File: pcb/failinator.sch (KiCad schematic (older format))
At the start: 5 parts, among them P1 CONN_01X04, P4 CONN_01X06, U2 RASPIPLUSHEADER, U3 LDS-CD16RI, U4 LDS-CD16RI

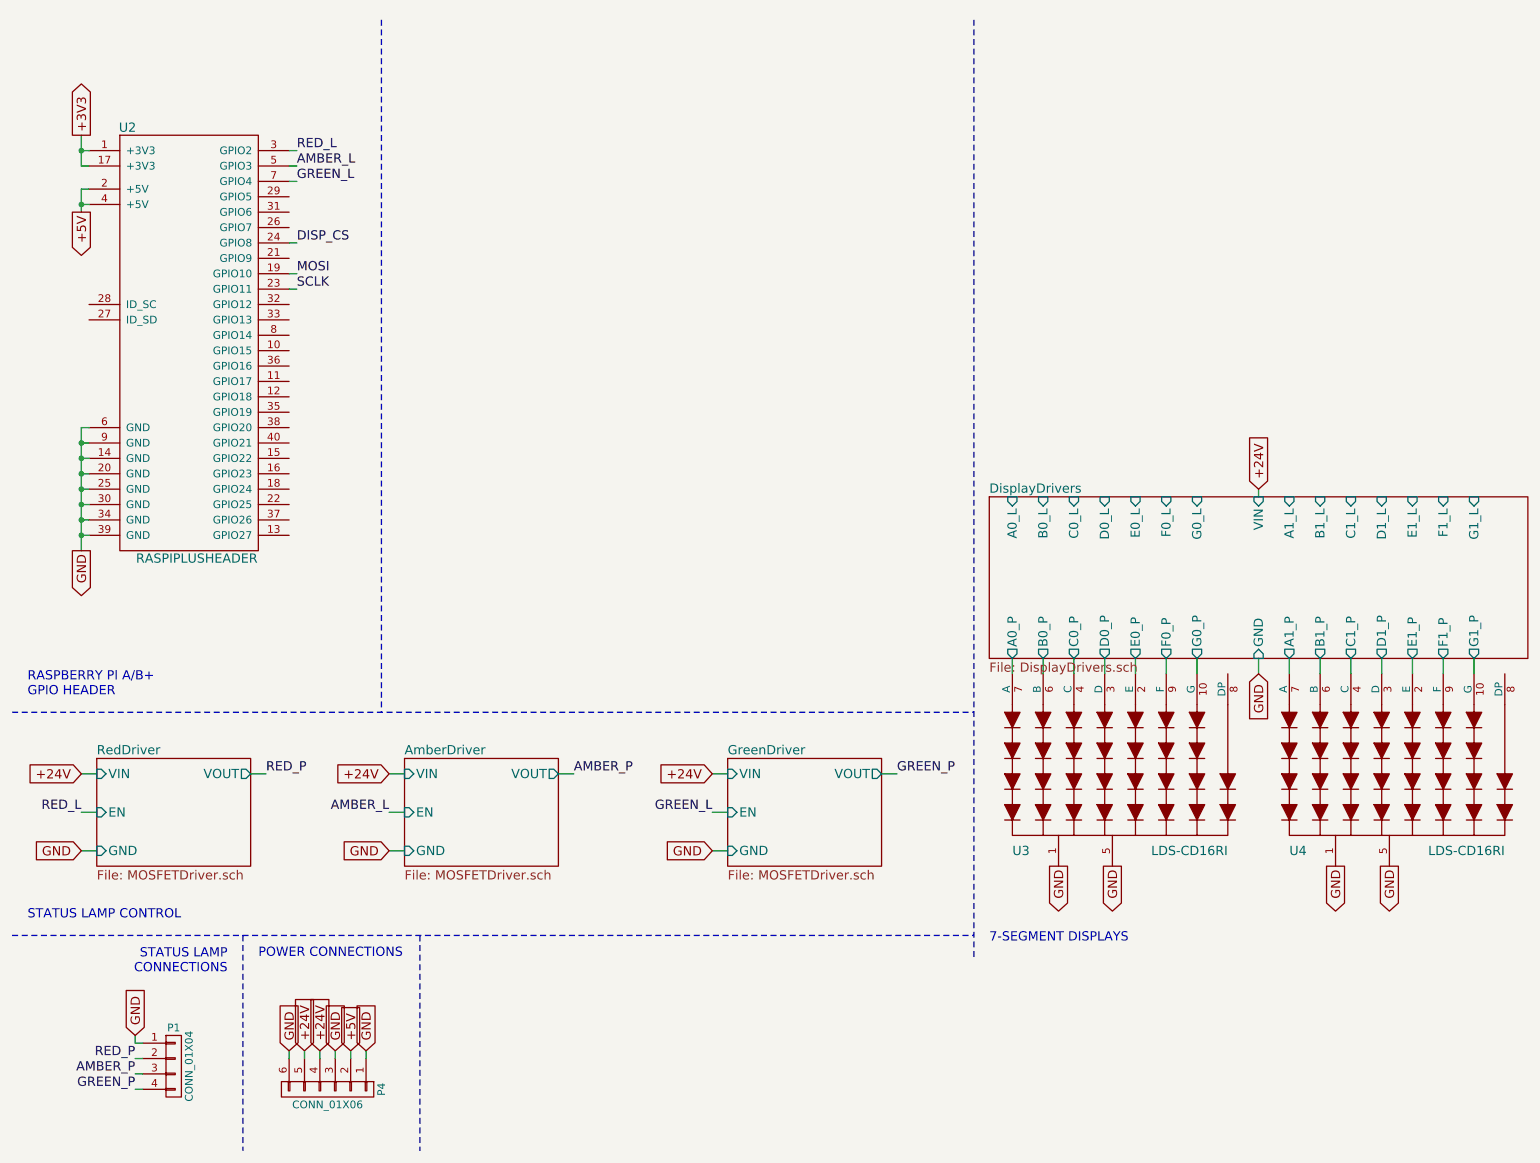
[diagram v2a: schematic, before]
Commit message: Shift registers for the 7-seg displays
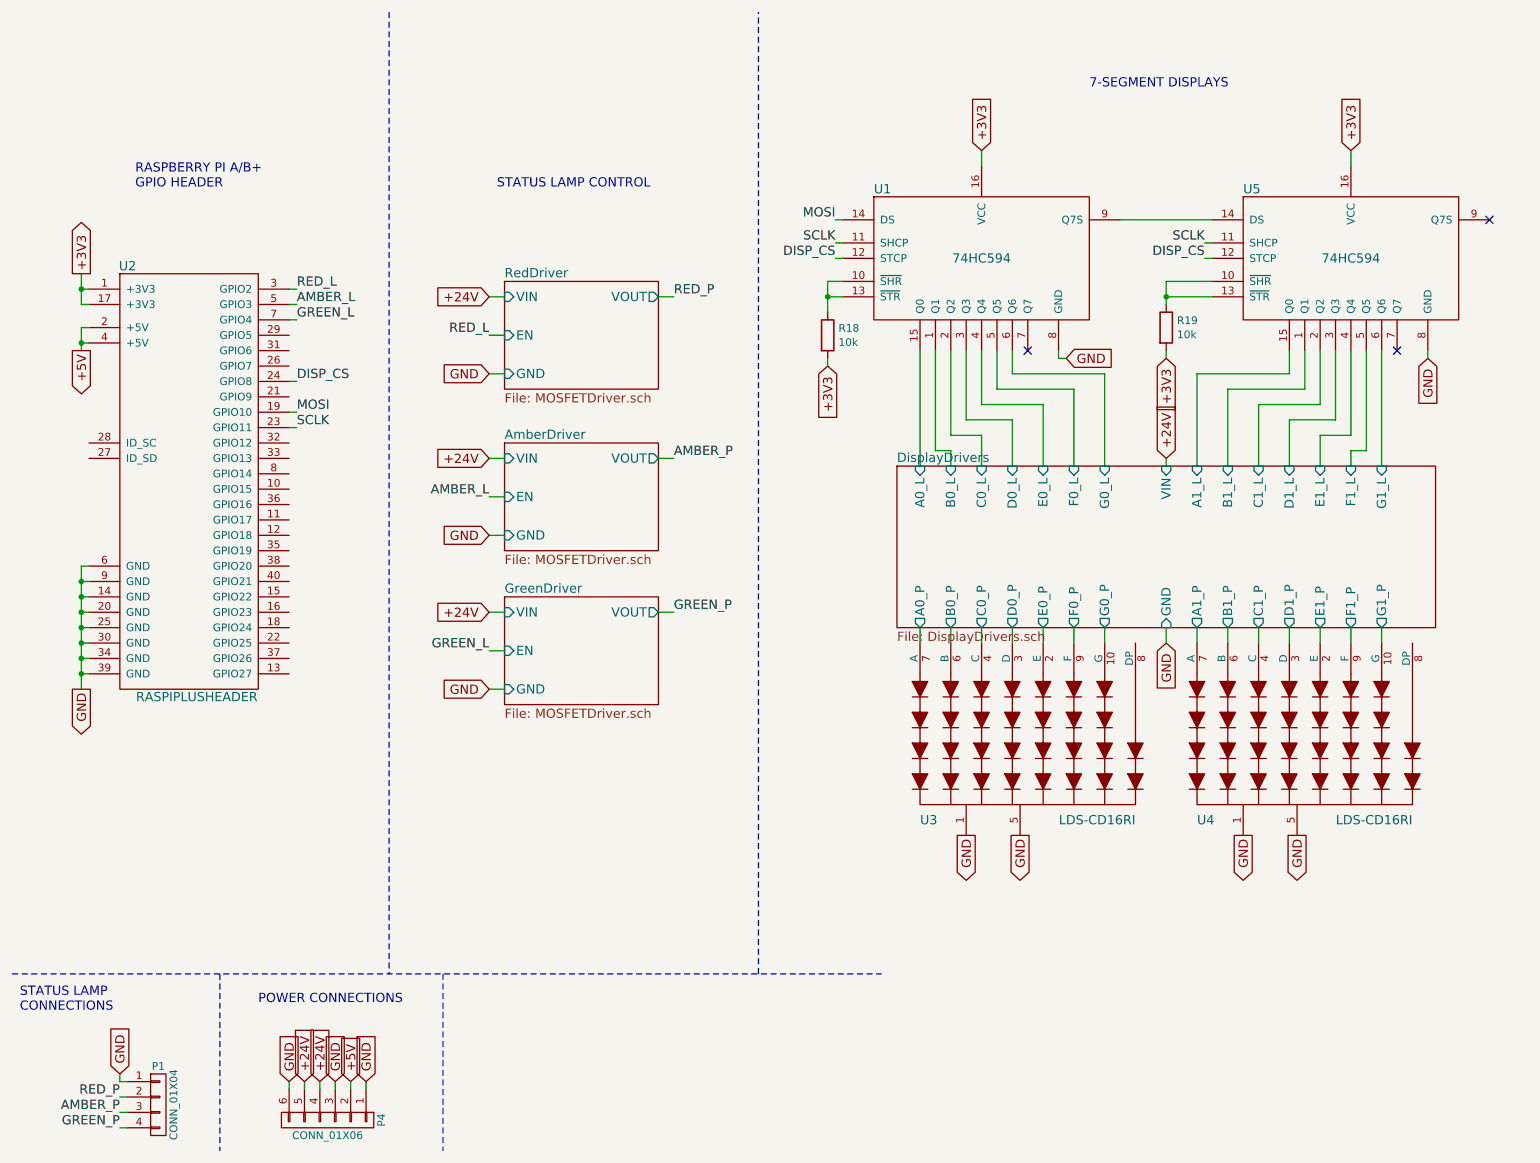
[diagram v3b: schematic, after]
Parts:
- added R18, R19: 10k, symbol R
- added U1, U5: 74HC594, symbol 74HC594
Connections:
- net +3V3: now also R18.2, R19.2, U1.16 (VCC), U5.16 (VCC)
- net DISP_CS: now also U1.12 (STCP), U5.12 (STCP)
- net DisplayDrivers/A0_L: now also U1.15 (Q0)
- net DisplayDrivers/A1_L: now also U5.15 (Q0)
- net DisplayDrivers/B0_L: now also U1.1 (Q1)
- net DisplayDrivers/B1_L: now also U5.1 (Q1)
- net DisplayDrivers/C0_L: now also U1.2 (Q2)
- net DisplayDrivers/C1_L: now also U5.2 (Q2)
- net DisplayDrivers/D0_L: now also U1.3 (Q3)
- net DisplayDrivers/D1_L: now also U5.3 (Q3)
- net DisplayDrivers/E0_L: now also U1.4 (Q4)
- net DisplayDrivers/E1_L: now also U5.4 (Q4)
- net DisplayDrivers/F0_L: now also U1.5 (Q5)
- net DisplayDrivers/F1_L: now also U5.5 (Q5)
- net DisplayDrivers/G0_L: now also U1.6 (Q6)
- net DisplayDrivers/G1_L: now also U5.6 (Q6)
- net GND: now also U1.8 (GND), U5.8 (GND)
- net MOSI: now also U1.14 (DS)
- net SCLK: now also U1.11 (SHCP), U5.11 (SHCP)
- new net: R18.1, U1.10 (~SHR), U1.13 (~STR)
- new net: U1.9 (Q7S), U5.14 (DS)
- new net: R19.1, U5.10 (~SHR), U5.13 (~STR)
- no-connect marks 0 -> 3
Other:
- moved on the sheet: P1, P4, U2, U3, U4

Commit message: Display board connects via 6-wire connector
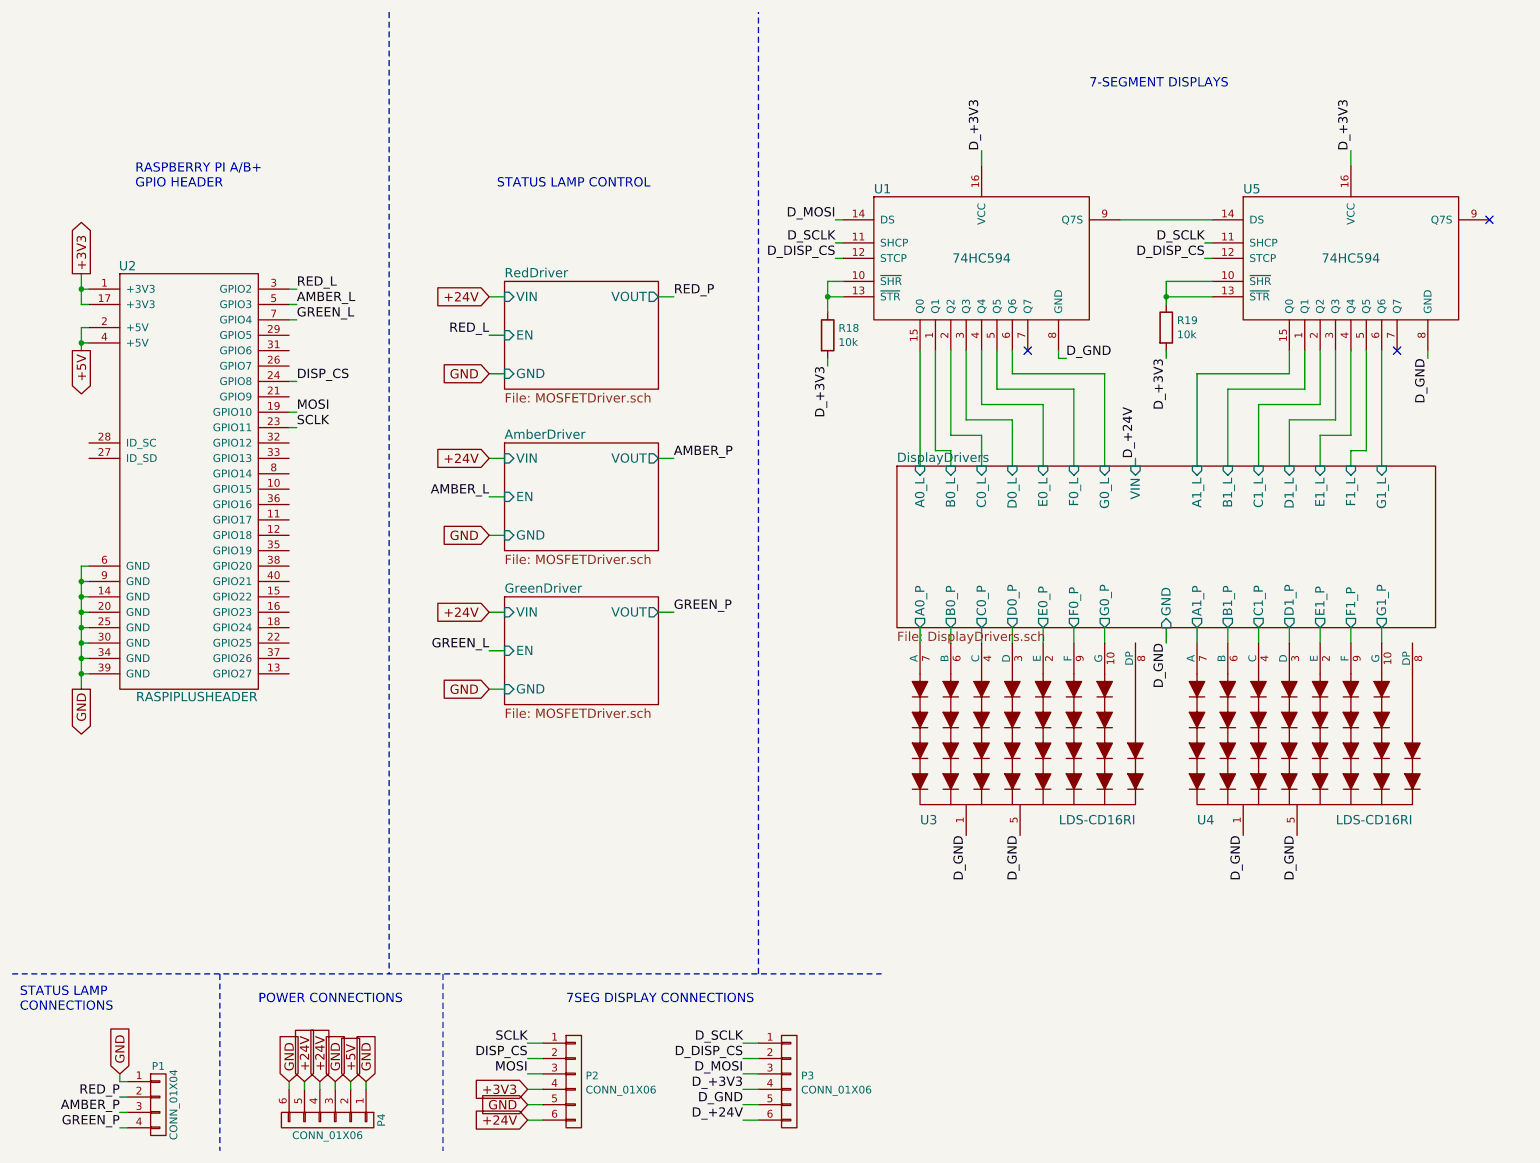
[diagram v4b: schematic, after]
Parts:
- added P2, P3: CONN_01X06, symbol CONN_01X06
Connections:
- net +24V: now also P2.6 (P6)
- net +3V3: now also P2.4 (P4); no longer R18.2, R19.2, U1.16 (VCC), U5.16 (VCC)
- net DISP_CS: now also P2.2 (P2); no longer U1.12 (STCP), U5.12 (STCP)
- net GND: now also P2.5 (P5); no longer U1.8 (GND), U3.1, U3.5, U4.1, U4.5, U5.8 (GND)
- net MOSI: now also P2.3 (P3); no longer U1.14 (DS)
- net SCLK: now also P2.1 (P1); no longer U1.11 (SHCP), U5.11 (SHCP)
- new net D_+24V: P3.6 (P6)
- new net D_+3V3: P3.4 (P4), R18.2, R19.2, U1.16 (VCC), U5.16 (VCC)
- new net D_DISP_CS: P3.2 (P2), U1.12 (STCP), U5.12 (STCP)
- new net D_GND: P3.5 (P5), U1.8 (GND), U3.1, U3.5, U4.1, U4.5, U5.8 (GND)
- new net D_MOSI: P3.3 (P3), U1.14 (DS)
- new net D_SCLK: P3.1 (P1), U1.11 (SHCP), U5.11 (SHCP)
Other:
- note added: "7SEG DISPLAY CONNECTIONS"
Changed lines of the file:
@@
 	1    0    0    -1
 $EndComp
-Text GLabel 6750 5900 3    60   Output ~ 0
-GND
-Text GLabel 7100 5900 3    60   Output ~ 0
-GND
 $Comp
 L LDS-CD16RI U4
@@
 	1    0    0    -1
 $EndComp
-Text GLabel 8550 5900 3    60   Output ~ 0
-GND
-Text GLabel 8900 5900 3    60   Output ~ 0
-GND
 Text Notes 7550 1050 0    60   ~ 0
 7-SEGMENT DISPLAYS
-Text GLabel 8050 4650 3    60   Input ~ 0
-GND
-Text GLabel 8050 3450 1    60   Input ~ 0
-+24V
 $Sheet
 S 6300 3500 3500 1050
@@
 F0 "DisplayDrivers" 60
 F1 "DisplayDrivers.sch" 60
-F2 "VIN" I T 8050 3500 60
+F2 "VIN" I T 7850 3500 60
 F3 "GND" I B 8050 4550 60
 F4 "A0_L" I T 6450 3500 60
@@
 	1    0    0    -1
 $EndComp
-Text GLabel 7400 2800 2    60   Input ~ 0
-GND
-Text GLabel 6850 1450 1    60   Input ~ 0
-+3V3
-Text GLabel 9250 1450 1    60   Input ~ 0
-+3V3
-Text GLabel 9750 2800 3    60   Input ~ 0
-GND
 NoConn ~ 9550 2750
 NoConn ~ 7150 2750
 NoConn ~ 10150 1900
 Text Label 5900 1900 2    60   ~ 0
-MOSI
+D_MOSI
 Text Label 5900 2050 2    60   ~ 0
-SCLK
+D_SCLK
 Text Label 5900 2150 2    60   ~ 0
-DISP_CS
+D_DISP_CS
 Text Label 8300 2050 2    60   ~ 0
-SCLK
+D_SCLK
 Text Label 8300 2150 2    60   ~ 0
-DISP_CS
-Text GLabel 8050 2800 3    60   Input ~ 0
-+3V3
-Text GLabel 5850 2850 3    60   Input ~ 0
-+3V3
+D_DISP_CS
 $Comp
 L R R18
@@
 Wire Wire Line
 	9450 4550 9450 4650
-Wire Wire Line
-	8050 3450 8050 3500
 Wire Wire Line
 	6450 3500 6450 2750
@@
 Wire Notes Line
 	3350 6800 3350 7950
+$Comp
+L CONN_01X06 P3
+U 1 1 56C94215
+P 5600 7500
+F 0 "P3" H 5677 7538 50  0000 L CNN
+F 1 "CONN_01X06" H 5677 7446 50  0000 L CNN
+F 2 "" H 5600 7500 50  0000 C CNN
+F 3 "" H 5600 7500 50  0000 C CNN
+	1    5600 7500
+	1    0    0    -1
+$EndComp
+$Comp
+L CONN_01X06 P2
+U 1 1 56C942DE
+P 4200 7500
+F 0 "P2" H 4277 7538 50  0000 L CNN
+F 1 "CONN_01X06" H 4277 7446 50  0000 L CNN
+F 2 "" H 4200 7500 50  0000 C CNN
+F 3 "" H 4200 7500 50  0000 C CNN
+	1    4200 7500
+	1    0    0    -1
+$EndComp
+Text GLabel 3900 7750 0    60   Input ~ 0
++24V
+Text GLabel 3900 7650 0    60   Input ~ 0
+GND
+Text GLabel 3900 7550 0    60   Input ~ 0
++3V3
+Text Label 3900 7450 2    60   ~ 0
+MOSI
+Text Label 3900 7350 2    60   ~ 0
+DISP_CS
+Text Label 3900 7250 2    60   ~ 0
+SCLK
+Wire Wire Line
+	3900 7250 4000 7250
+Wire Wire Line
+	3900 7350 4000 7350
+Wire Wire Line
+	3900 7450 4000 7450
+Wire Wire Line
+	3900 7550 4000 7550
+Wire Wire Line
+	3900 7650 4000 7650
+Wire Wire Line
+	3900 7750 4000 7750
+Text Label 5300 7250 2    60   ~ 0
+D_SCLK
+Text Label 5300 7350 2    60   ~ 0
+D_DISP_CS
+Text Label 5300 7450 2    60   ~ 0
+D_MOSI
+Text Label 5300 7550 2    60   ~ 0
+D_+3V3
+Text Label 5300 7650 2    60   ~ 0
+D_GND
+Text Label 5300 7750 2    60   ~ 0
+D_+24V
+Wire Wire Line
+	5300 7250 5400 7250
+Wire Wire Line
+	5300 7350 5400 7350
+Wire Wire Line
+	5300 7450 5400 7450
+Wire Wire Line
+	5300 7550 5400 7550
+Wire Wire Line
+	5300 7650 5400 7650
+Wire Wire Line
+	5300 7750 5400 7750
+Text Notes 4150 7000 0    60   ~ 0
+7SEG DISPLAY CONNECTIONS
+Text Label 6850 1450 1    60   ~ 0
+D_+3V3
+Text Label 9250 1450 1    60   ~ 0
+D_+3V3
+Text Label 5850 2850 3    60   ~ 0
+D_+3V3
+Text Label 8050 2800 3    60   ~ 0
+D_+3V3
+Text Label 7850 3450 1    60   ~ 0
+D_+24V
+Wire Wire Line
+	7850 3450 7850 3500
+Text Label 7400 2800 0    60   ~ 0
+D_GND
+Text Label 9750 2800 3    60   ~ 0
+D_GND
+Text Label 6750 5900 3    60   ~ 0
+D_GND
+Text Label 7100 5900 3    60   ~ 0
+D_GND
+Text Label 8550 5900 3    60   ~ 0
+D_GND
+Text Label 8900 5900 3    60   ~ 0
+D_GND
+Text Label 8050 4650 3    60   ~ 0
+D_GND
 $EndSCHEMATC

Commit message: Shift register decoupling caps
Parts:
- added C1, C2: C_Small, symbol C_Small
- R18, R19: footprint (none) -> Resistors_SMD:R_0805_HandSoldering
- U1, U5: footprint (none) -> Housings_SOIC:SOIC-16_3.9x9.9mm_Pitch1.27mm
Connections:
- net D_+3V3: now also C1.2, C2.2
- net D_GND: now also C1.1, C2.1
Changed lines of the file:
@@
 P 6850 2150
 F 0 "U1" H 6150 2600 60  0000 L CNN
-F 1 "74HC594" H 6850 2150 60  0000 C CNN
-F 2 "" H 6400 2100 60  0000 C CNN
+F 1 "74HC594" H 6650 2150 60  0000 L CNN
+F 2 "Housings_SOIC:SOIC-16_3.9x9.9mm_Pitch1.27mm" H 7050 2700 60  0001 L CNN
 F 3 "" H 6400 2100 60  0000 C CNN
 	1    6850 2150
@@
 F 0 "U5" H 8550 2600 60  0000 L CNN
 F 1 "74HC594" H 9250 2150 60  0000 C CNN
-F 2 "" H 8800 2100 60  0000 C CNN
+F 2 "Housings_SOIC:SOIC-16_3.9x9.9mm_Pitch1.27mm" H 8800 2100 60  0001 C CNN
 F 3 "" H 8800 2100 60  0000 C CNN
 	1    9250 2150
@@
 F 0 "R18" H 5920 2696 50  0000 L CNN
 F 1 "10k" H 5920 2604 50  0000 L CNN
-F 2 "" V 5780 2650 50  0000 C CNN
+F 2 "Resistors_SMD:R_0805_HandSoldering" H 5920 2558 50  0001 L CNN
 F 3 "" H 5850 2650 50  0000 C CNN
 	1    5850 2650
@@
 F 0 "R19" H 8120 2646 50  0000 L CNN
 F 1 "10k" H 8120 2554 50  0000 L CNN
-F 2 "" V 7980 2600 50  0000 C CNN
+F 2 "Resistors_SMD:R_0805_HandSoldering" V 7980 2600 50  0001 C CNN
 F 3 "" H 8050 2600 50  0000 C CNN
 	1    8050 2600
@@
 Text Label 8050 4650 3    60   ~ 0
 D_GND
+$Comp
+L C_Small C2
+U 1 1 56C9F0BA
+P 6050 6450
+F 0 "C2" V 6300 6450 50  0000 C CNN
+F 1 "C_Small" V 6200 6450 50  0000 C CNN
+F 2 "" H 6050 6450 50  0000 C CNN
+F 3 "" H 6050 6450 50  0000 C CNN
+	1    6050 6450
+	0    1    1    0
+$EndComp
+$Comp
+L C_Small C1
+U 1 1 56C9F3F1
+P 6050 6250
+F 0 "C1" V 5800 6250 50  0000 C CNN
+F 1 "C_Small" V 5900 6250 50  0000 C CNN
+F 2 "" H 6050 6250 50  0000 C CNN
+F 3 "" H 6050 6250 50  0000 C CNN
+	1    6050 6250
+	0    1    1    0
+$EndComp
+Text Label 6300 6350 0    60   ~ 0
+D_GND
+Text Label 5800 6350 2    60   ~ 0
+D_+3V3
+Wire Wire Line
+	5800 6350 5850 6350
+Wire Wire Line
+	5850 6250 5850 6450
+Wire Wire Line
+	5850 6250 5950 6250
+Wire Wire Line
+	6150 6250 6250 6250
+Wire Wire Line
+	6250 6250 6250 6450
+Wire Wire Line
+	6250 6350 6300 6350
+Wire Wire Line
+	5850 6450 5950 6450
+Connection ~ 5850 6350
+Wire Wire Line
+	6250 6450 6150 6450
+Connection ~ 6250 6350
 $EndSCHEMATC

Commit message: Some footprint assignments
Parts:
- C1, C2: footprint (none) -> Capacitors_SMD:C_0805_HandSoldering
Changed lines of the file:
@@
 F 0 "U3" H 6450 4700 60  0000 L CNN
 F 1 "LDS-CD16RI" H 7850 4700 60  0000 R CNN
-F 2 "" H 6900 5650 60  0000 C CNN
+F 2 "" H 6900 5650 60  0001 C CNN
 F 3 "" H 6900 5650 60  0000 C CNN
 	1    7150 5250
@@
 F 0 "U4" H 8250 4700 60  0000 L CNN
 F 1 "LDS-CD16RI" H 9650 4700 60  0000 R CNN
-F 2 "" H 8700 5650 60  0000 C CNN
+F 2 "" H 8700 5650 60  0001 C CNN
 F 3 "" H 8700 5650 60  0000 C CNN
 	1    8950 5250
@@
 F 0 "P3" H 5677 7538 50  0000 L CNN
 F 1 "CONN_01X06" H 5677 7446 50  0000 L CNN
-F 2 "" H 5600 7500 50  0000 C CNN
+F 2 "" H 5600 7500 50  0001 C CNN
 F 3 "" H 5600 7500 50  0000 C CNN
 	1    5600 7500
@@
 F 0 "P2" H 4277 7538 50  0000 L CNN
 F 1 "CONN_01X06" H 4277 7446 50  0000 L CNN
-F 2 "" H 4200 7500 50  0000 C CNN
+F 2 "" H 4200 7500 50  0001 C CNN
 F 3 "" H 4200 7500 50  0000 C CNN
 	1    4200 7500
@@
 F 0 "C2" V 6300 6450 50  0000 C CNN
 F 1 "C_Small" V 6200 6450 50  0000 C CNN
-F 2 "" H 6050 6450 50  0000 C CNN
+F 2 "Capacitors_SMD:C_0805_HandSoldering" H 6050 6450 50  0001 C CNN
 F 3 "" H 6050 6450 50  0000 C CNN
 	1    6050 6450
@@
 F 0 "C1" V 5800 6250 50  0000 C CNN
 F 1 "C_Small" V 5900 6250 50  0000 C CNN
-F 2 "" H 6050 6250 50  0000 C CNN
+F 2 "Capacitors_SMD:C_0805_HandSoldering" H 6050 6250 50  0001 C CNN
 F 3 "" H 6050 6250 50  0000 C CNN
 	1    6050 6250

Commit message: Remaining footprint assignments
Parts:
- P2: footprint (none) -> failinator:Wire_Conn_6pin_StrainReliefRight
- P3: footprint (none) -> Pin_Headers:Pin_Header_Straight_1x06
- U3, U4: footprint (none) -> failinator:LDS-CD16RI
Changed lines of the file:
@@
 F 0 "U3" H 6450 4700 60  0000 L CNN
 F 1 "LDS-CD16RI" H 7850 4700 60  0000 R CNN
-F 2 "" H 6900 5650 60  0001 C CNN
+F 2 "failinator:LDS-CD16RI" H 6900 5650 60  0001 C CNN
 F 3 "" H 6900 5650 60  0000 C CNN
 	1    7150 5250
@@
 F 0 "U4" H 8250 4700 60  0000 L CNN
 F 1 "LDS-CD16RI" H 9650 4700 60  0000 R CNN
-F 2 "" H 8700 5650 60  0001 C CNN
+F 2 "failinator:LDS-CD16RI" H 8700 5650 60  0001 C CNN
 F 3 "" H 8700 5650 60  0000 C CNN
 	1    8950 5250
@@
 F 0 "P3" H 5677 7538 50  0000 L CNN
 F 1 "CONN_01X06" H 5677 7446 50  0000 L CNN
-F 2 "" H 5600 7500 50  0001 C CNN
+F 2 "Pin_Headers:Pin_Header_Straight_1x06" H 5600 7500 50  0001 C CNN
 F 3 "" H 5600 7500 50  0000 C CNN
 	1    5600 7500
@@
 F 0 "P2" H 4277 7538 50  0000 L CNN
 F 1 "CONN_01X06" H 4277 7446 50  0000 L CNN
-F 2 "" H 4200 7500 50  0001 C CNN
+F 2 "failinator:Wire_Conn_6pin_StrainReliefRight" H 4200 7500 50  0001 C CNN
 F 3 "" H 4200 7500 50  0000 C CNN
 	1    4200 7500

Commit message: Use through-hole footprints for all display board resistors
Previously two of them were incorrectly set to 0805 SMD footprints.

I actually expect the display board layout is going to be very cramped
so these might actually all become 0805s later, but going to try with
through-hole first because I don't relish the thought of hand-soldering
14 0805 resistors in a single sitting.
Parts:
- R18, R19: footprint Resistors_SMD:R_0805_HandSoldering -> Discret:R3
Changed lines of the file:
@@
 F 0 "R18" H 5920 2696 50  0000 L CNN
 F 1 "10k" H 5920 2604 50  0000 L CNN
-F 2 "Resistors_SMD:R_0805_HandSoldering" H 5920 2558 50  0001 L CNN
+F 2 "Discret:R3" H 5920 2558 50  0001 L CNN
 F 3 "" H 5850 2650 50  0000 C CNN
 	1    5850 2650
@@
 F 0 "R19" H 8120 2646 50  0000 L CNN
 F 1 "10k" H 8120 2554 50  0000 L CNN
-F 2 "Resistors_SMD:R_0805_HandSoldering" V 7980 2600 50  0001 C CNN
+F 2 "Discret:R3" V 7980 2600 50  0001 C CNN
 F 3 "" H 8050 2600 50  0000 C CNN
 	1    8050 2600
